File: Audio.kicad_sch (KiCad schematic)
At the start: 15 parts, among them J5 AudioJack, U12 PCM5121PW, U13 TLV74033PDBVR

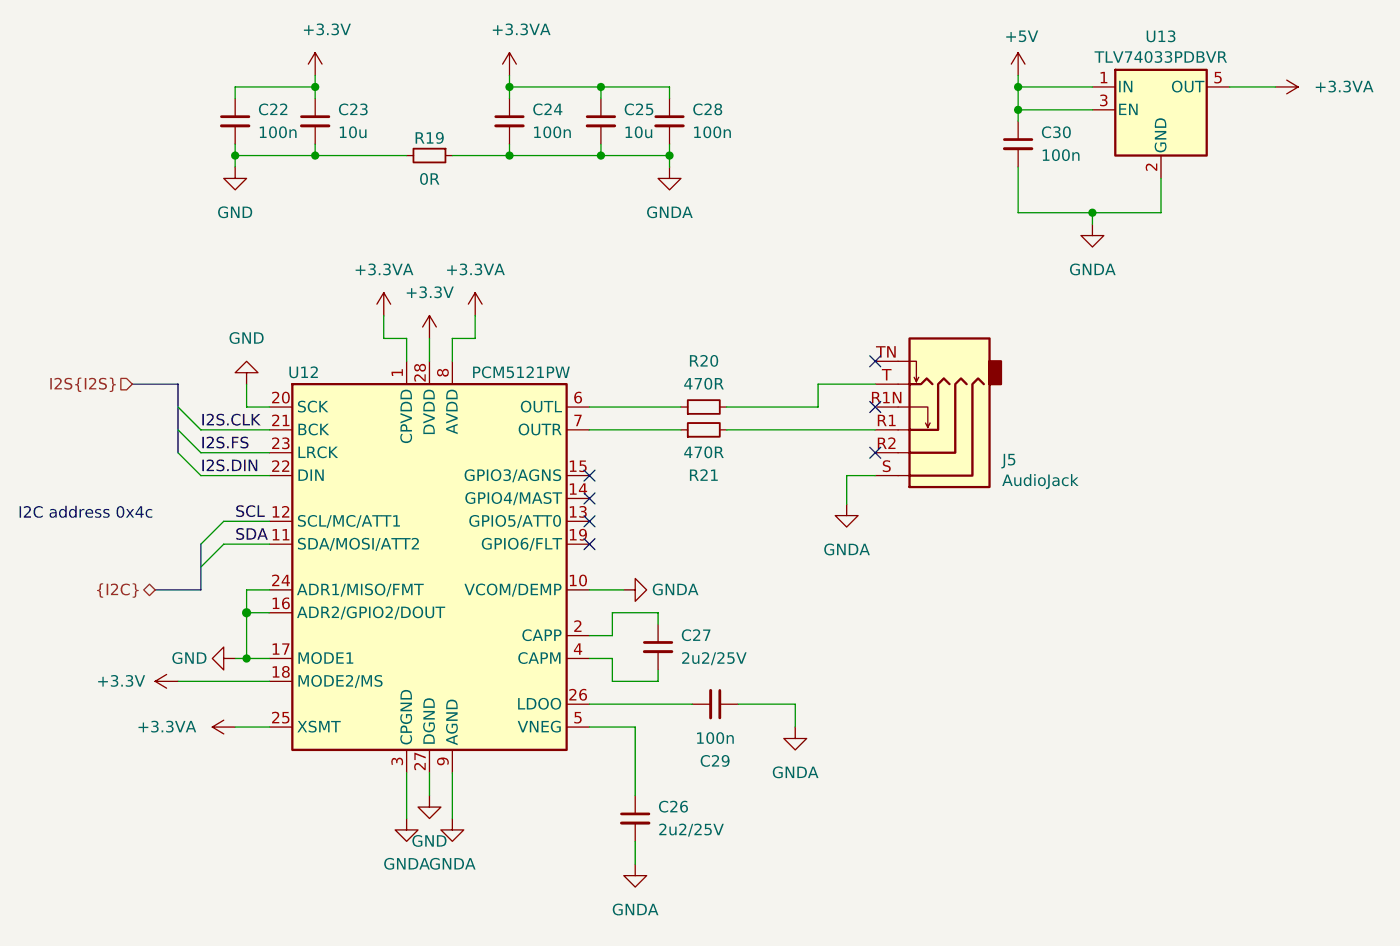
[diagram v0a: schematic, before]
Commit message: initial rev 0.3:
updates
schematic:
-change usb current protection IC to 1.5A
-Added low-pass filter to the audio output
-PoE fixed primary windings polarity
-added option to select poe class with a jumper (between 3 and 4)
-fixes in poe design
-added testpoints
-added virtual hirose df40c connectors for pick and place use

lightblue.pretty:
-added fake DF40C footprint for pick and place and 3d model purposes

Signed-off-by: Dominik Sliwa <dominik@sliwa.io>
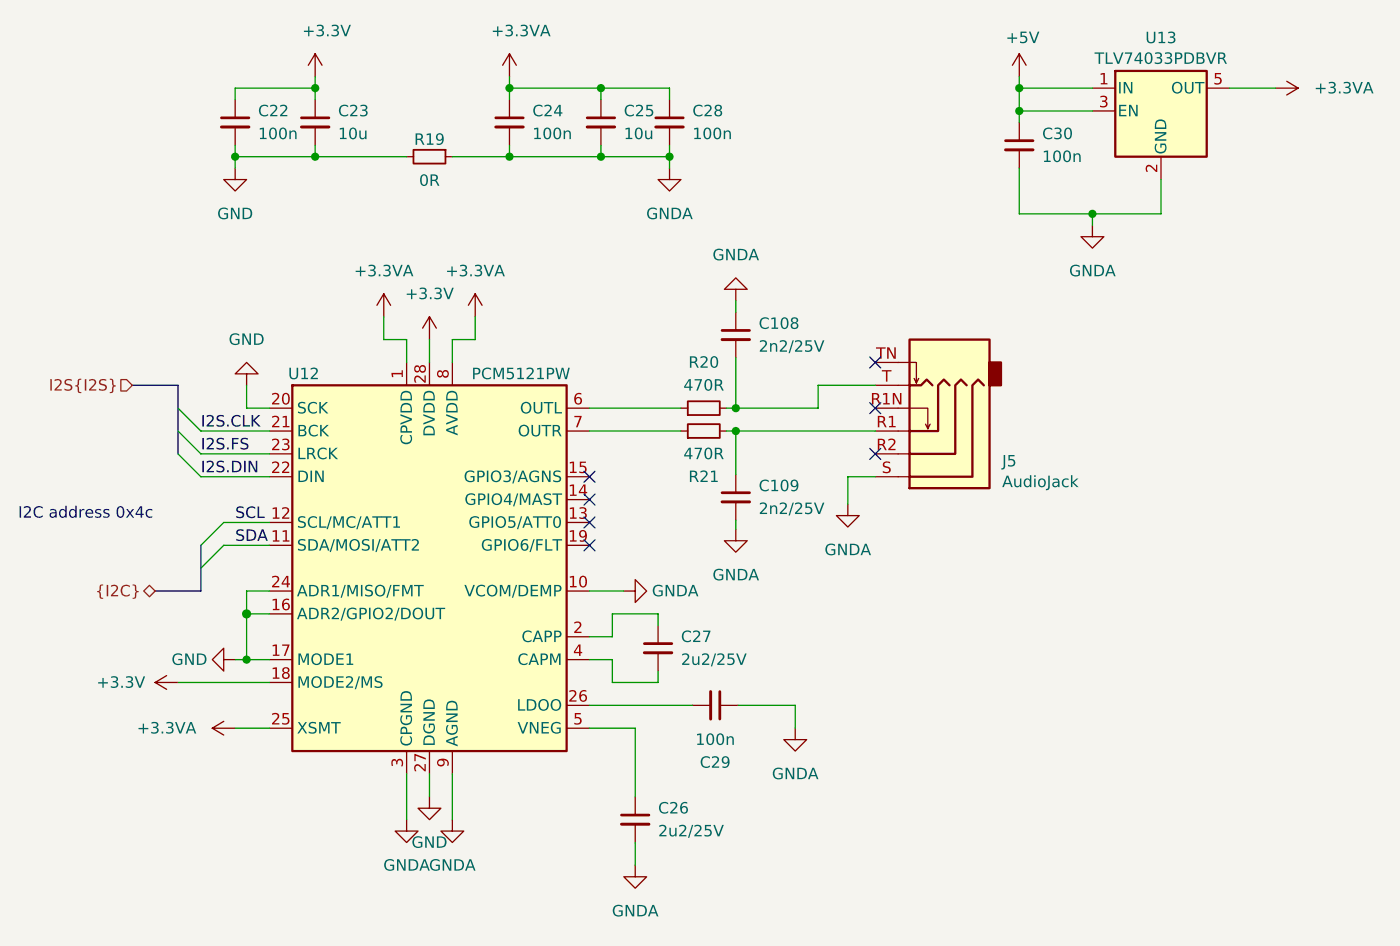
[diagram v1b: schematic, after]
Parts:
- added C108, C109: 2n2/25V, Capacitor_SMD:C_0805_2012Metric, symbol Device:C_Small
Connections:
- net GNDA: now also C108.1, C109.2
- net at J5.R1, R21.2: now also C109.1
- net at J5.T, R20.2: now also C108.2

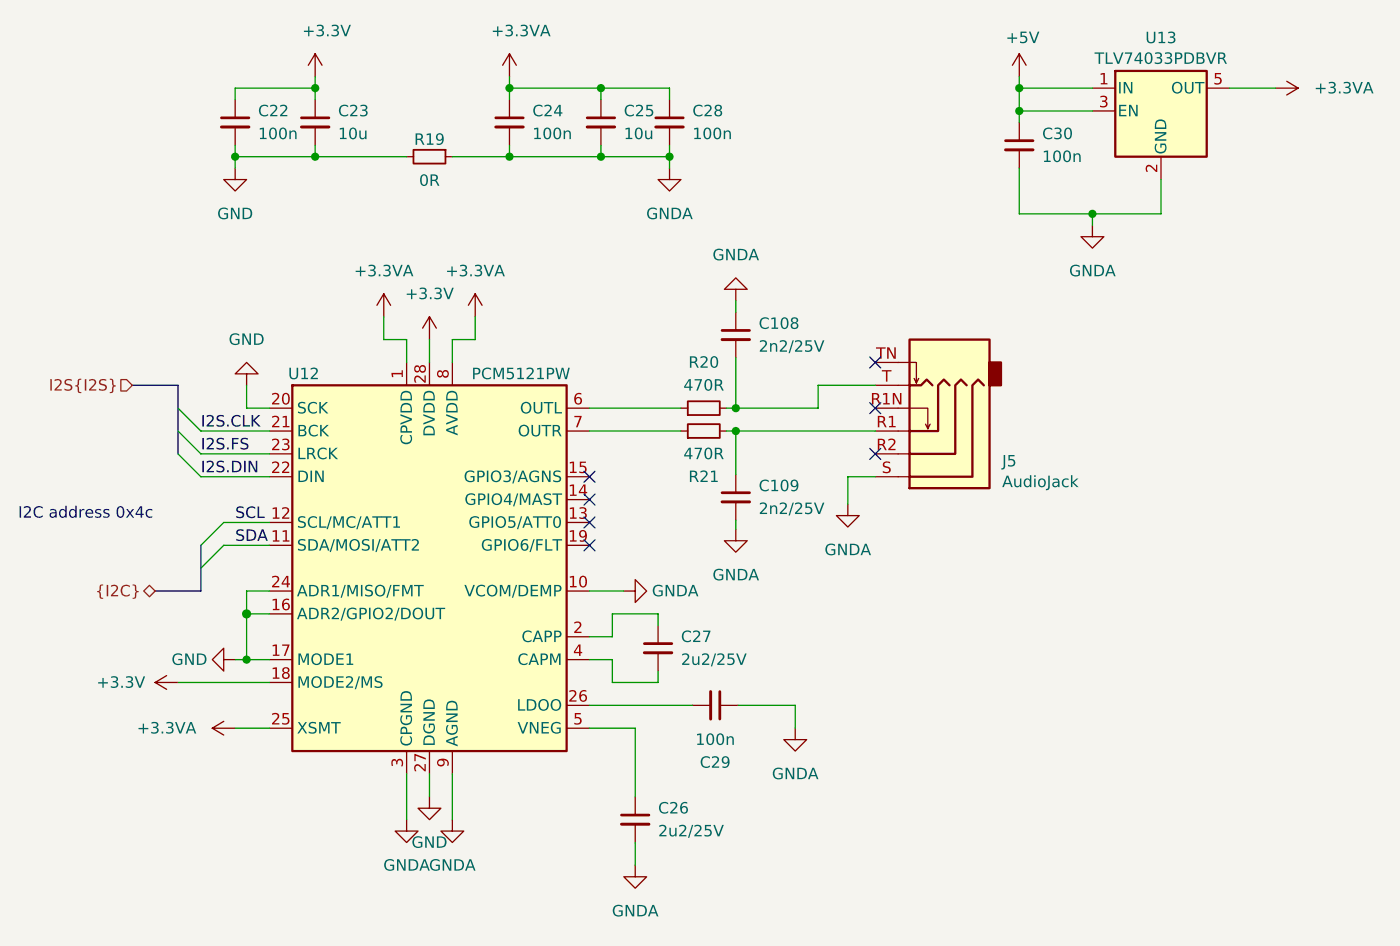
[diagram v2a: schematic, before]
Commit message: Use XKB-Connectivity PJ-3270 3.5mm Audio plug
Replace the HRO part with the XKB part. The HRO part had shorter feet
which caused issues during soldering.

Fixes: #30

Signed-off-by: Stefan Agner <stefan@agner.ch>
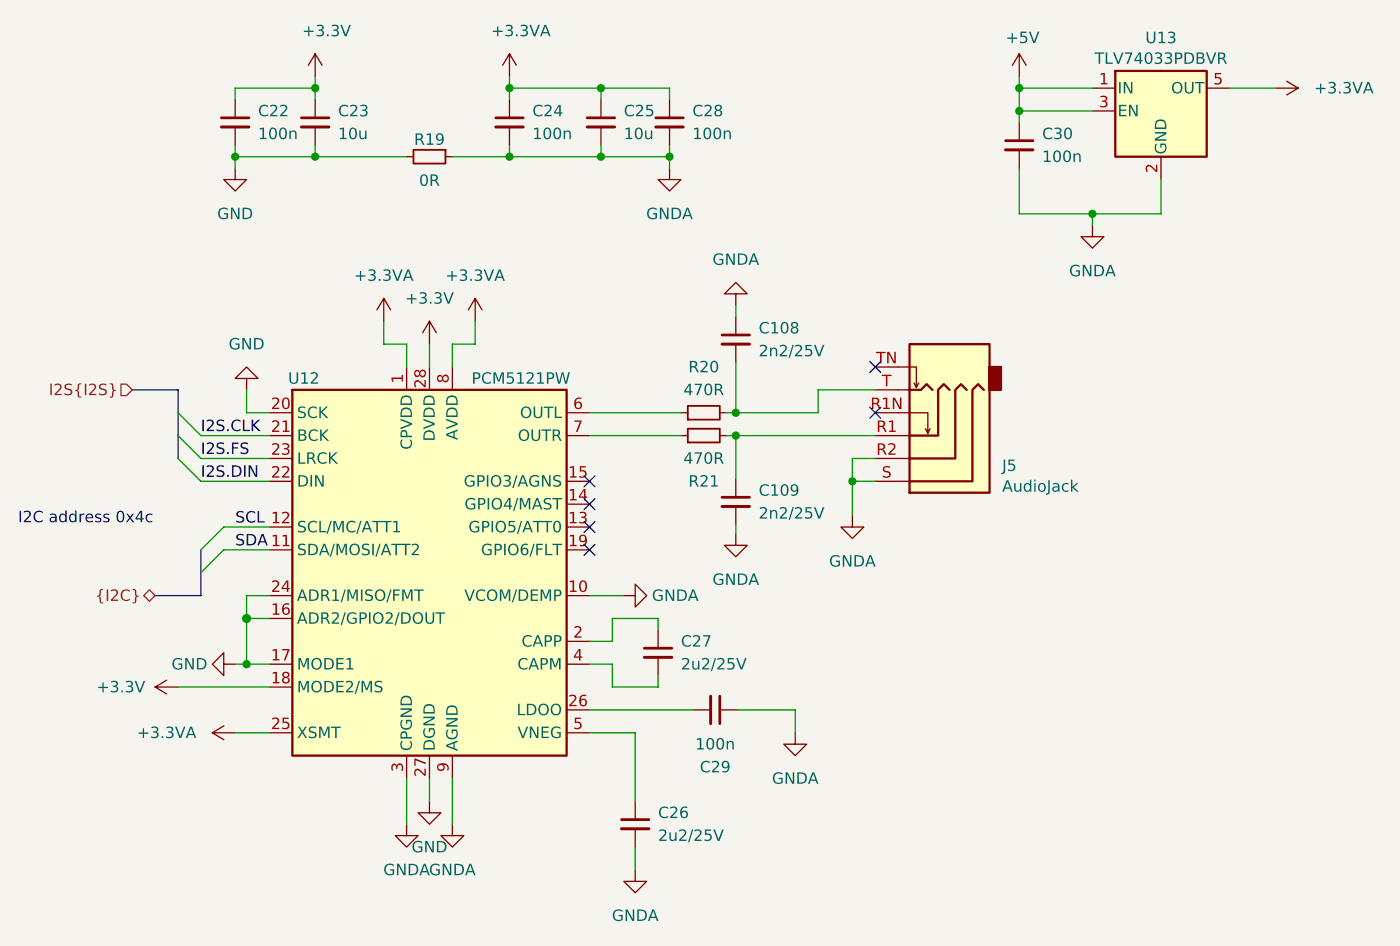
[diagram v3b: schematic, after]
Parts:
- J5: footprint LightBlue:Jack_3.5mm_HRO_PJ-3973-6A_Horizontal -> LightBlue:Jack_3.5mm_XKB_PJ-3270_Horizontal; Manufacturer HRO -> XKB Connectivity; PartNumber PJ-3973-6A -> PJ-3270
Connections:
- net GNDA: now also J5.R2
- no-connect marks 7 -> 6
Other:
- moved on the sheet: C108, C109, C26, C27, C29, J5, R20, R21, U12

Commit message: Renmae LightBlue to Amber
Signed-off-by: Stefan Agner <stefan@agner.ch>
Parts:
- J5: footprint LightBlue:Jack_3.5mm_XKB_PJ-3270_Horizontal -> Amber:Jack_3.5mm_XKB_PJ-3270_Horizontal
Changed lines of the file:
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@@
     (company "Nabu Casa")
     (comment 1 "www.nabucasa.com")
-    (comment 2 "Light Blue")
+    (comment 2 "Amber")
   )
   (bus_alias "I2S" (members "CLK" "FS" "DIN"))
@@
       (effects (font (size 1.27 1.27)) (justify right))
     )
-    (property "Footprint" "LightBlue:Jack_3.5mm_XKB_PJ-3270_Horizontal" (id 2) (at 166.37 83.82 0)
-      (effects (font (size 1.27 1.27)) hide)
-    )
+    (property "Footprint" "Amber:Jack_3.5mm_XKB_PJ-3270_Horizontal" (id 2) (at 166.37 83.82 0)
+      (effects (font (size 1.27 1.27)) hide)
+    )

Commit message: Changes to PoE for EMI compliance and improved efficiency
PoE
-Added a common mode filter on the input
-FB filter on the output side
-12V in now disables the poe with the DEN pin
-DT is now disabled
-PSRS is now disabled
-move to 1210 resistors for resistors identified in thermal testing
-DTHR is now enabled in default BoM
-some resistor values were adjusted
-some caps were moved to the common power supply section

USB:
-USB Hub 1.8V rail have capacitors added

Signed-off-by: Dominik Sliwa <dominik@sliwa.io>
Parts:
- R19: footprint Resistor_SMD:R_0402_1005Metric -> Resistor_SMD:R_1206_3216Metric
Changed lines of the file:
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@@
     (property "Reference" "R19" (id 0) (at 110.49 50.9208 90))
     (property "Value" "0R" (id 1) (at 110.49 55.48 90))
-    (property "Footprint" "Resistor_SMD:R_0402_1005Metric" (id 2) (at 110.49 52.832 0)
+    (property "Footprint" "Resistor_SMD:R_1206_3216Metric" (id 2) (at 110.49 52.832 0)
       (effects (font (size 1.27 1.27)) hide)
     )

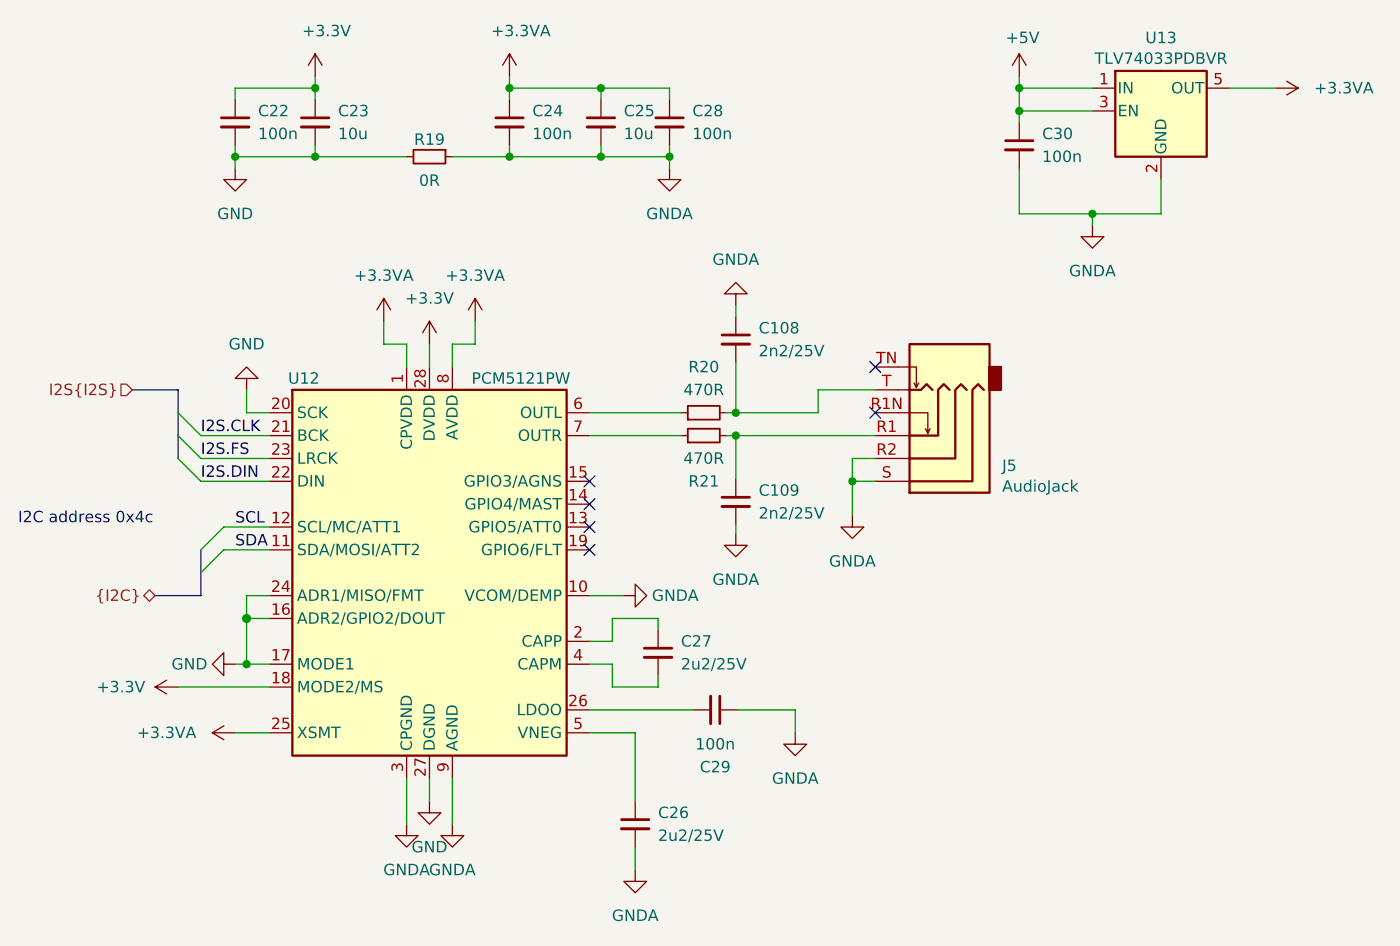
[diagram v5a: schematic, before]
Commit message: Remove GNDA, add audio/button ESD protection
Signed-off-by: Dominik Sliwa <dominik@sliwa.io>
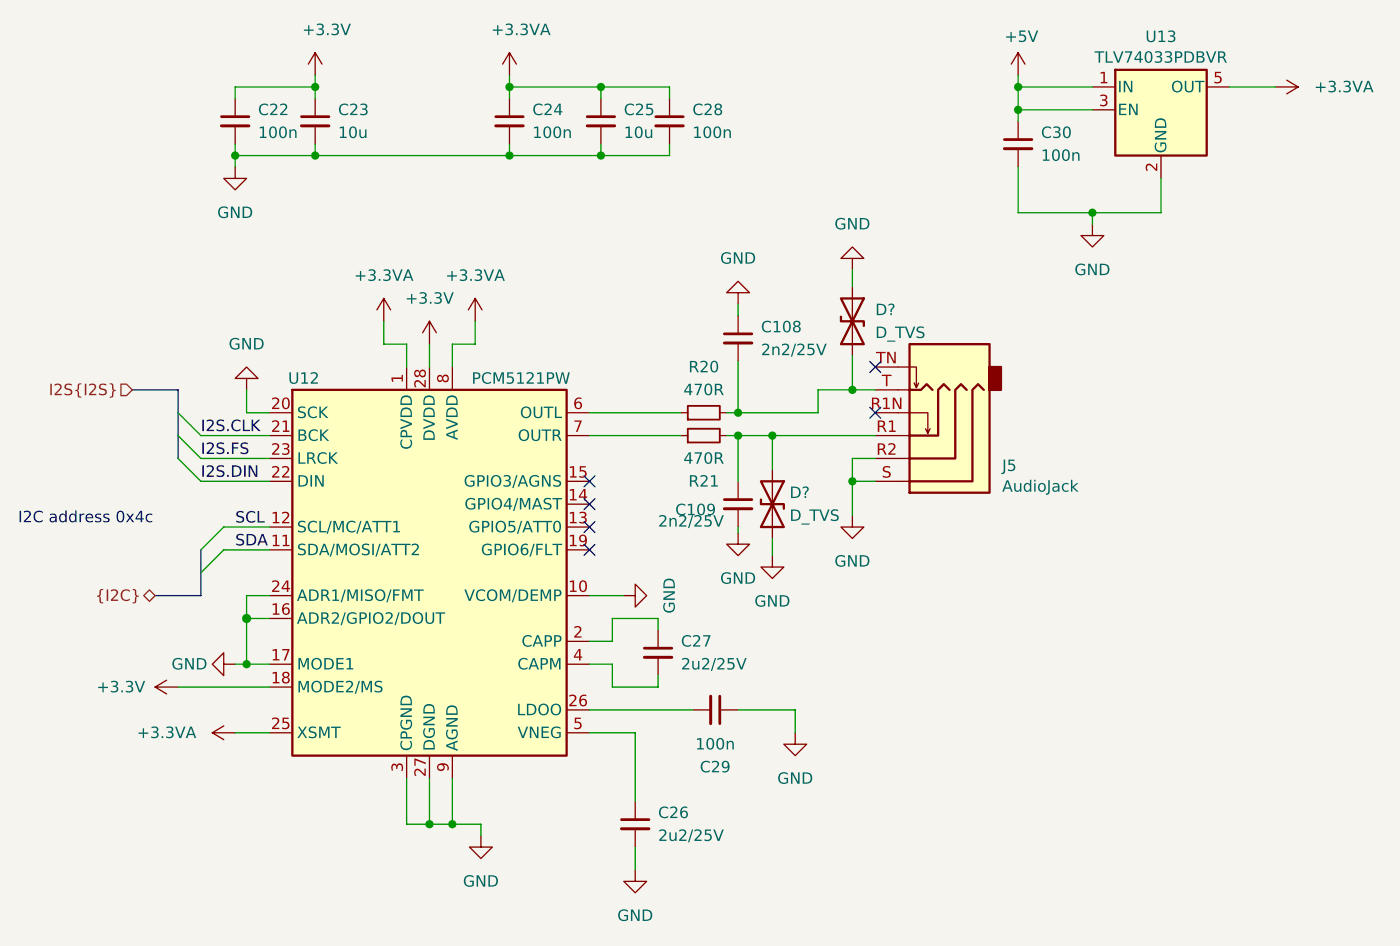
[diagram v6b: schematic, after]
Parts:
- removed R19: 0R, Resistor_SMD:R_1206_3216Metric, symbol Device:R_Small
- added D? (x2): D_TVS, symbol Device:D_TVS
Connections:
- net GNDA is gone; now on net GND: C108.1, C109.2, C24.2, C25.2, C26.2, C28.2, C29.1, C30.2, J5.R2, J5.S, U12.10 (VCOM/DEMP), U12.3 (CPGND), U12.9 (AGND), U13.2 (GND)
- net GND: now also D?.1 (A1), D?.2 (A2)
- net at C108.2, J5.T, R20.2: now also D?.2 (A2)
- net at C109.1, J5.R1, R21.2: now also D?.1 (A1)
